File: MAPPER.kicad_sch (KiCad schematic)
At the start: 27 parts

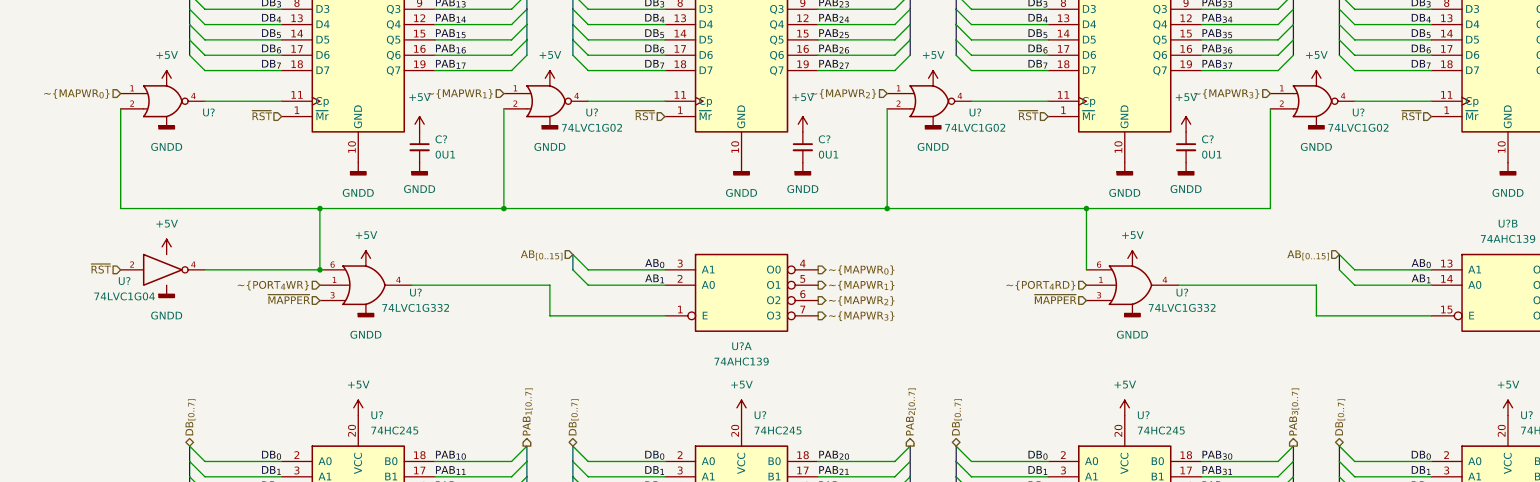
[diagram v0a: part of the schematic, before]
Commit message: distrustful of timing on reset of mapping registers
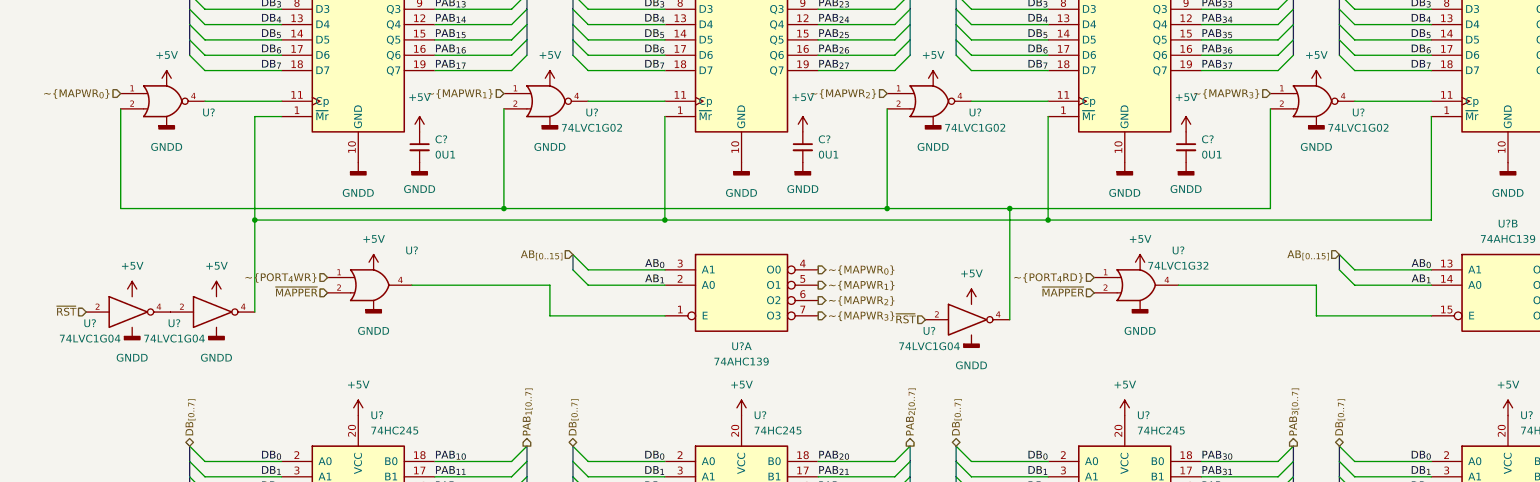
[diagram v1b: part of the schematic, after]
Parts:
- removed U? (x2): 74LVC1G332, symbol 74xGxx:74LVC1G332
- added U?: 74LVC1G32, symbol 74xGxx:74LVC1G32
- added U?: (no value), symbol 74xGxx:74LVC1G32
- added U? (x2): 74LVC1G04, symbol 74xGxx:74LVC1G04
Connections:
- net +5V: now also U?.5 (VCC), U?.5 (VCC), U?.5 (VCC), U?.5 (VCC)
- net GND: now also U?.3 (GND), U?.3 (GND), U?.3 (GND), U?.3 (GND)
- net ~{MAPPER}: now also U?.2, U?.2
- net ~{PORT_{4}RD}: now also U?.1
- net ~{PORT_{4}WR}: now also U?.1
- net ~{RST}: now also U?.2; no longer U?.1 (~{Mr}), U?.1 (~{Mr}), U?.1 (~{Mr}), U?.1 (~{Mr})
- net at U?.15 (E): now also U?.4
- net at U?.1 (E): now also U?.4
- new net: U?.1 (~{Mr}), U?.1 (~{Mr}), U?.1 (~{Mr}), U?.1 (~{Mr}), U?.4
- new net: U?.2, U?.4
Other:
- moved on the sheet: U?

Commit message: duh obvious optimization
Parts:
- removed U?: 74LVC1G04, symbol 74xGxx:74LVC1G04
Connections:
- net at U?.2, U?.2, U?.2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: now also U?.2, U?.4
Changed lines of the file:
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@@
   (junction (at 114.3 80.645) (diameter 0) (color 0 0 0 0)
   )
-  (junction (at 171.45 78.74) (diameter 0) (color 0 0 0 0)
-  )
   (junction (at 46.355 80.645) (diameter 0) (color 0 0 0 0)
   )
@@
   (junction (at 151.13 78.74) (diameter 0) (color 0 0 0 0)
   )
+  (junction (at 32.385 95.885) (diameter 0) (color 0 0 0 0)
+  )
+  (junction (at 32.385 78.74) (diameter 0) (color 0 0 0 0)
+  )
   (bus_entry (at 162.56 40.64) (size 2.54 2.54)
     (stroke (width 0) (type default) (color 0 0 0 0))
@@
     (stroke (width 0) (type default) (color 0 0 0 0))
   )
+  (wire (pts (xy 32.385 78.74) (xy 32.385 95.885))
+    (stroke (width 0) (type default) (color 0 0 0 0))
+  )
   (bus (pts (xy 35.56 118.11) (xy 35.56 120.65))
     (stroke (width 0) (type default) (color 0 0 0 0))
@@
     (stroke (width 0) (type default) (color 0 0 0 0))
   )
-  (wire (pts (xy 171.45 78.74) (xy 171.45 97.155))
-    (stroke (width 0) (type default) (color 0 0 0 0))
-  )
   (bus (pts (xy 218.44 133.35) (xy 218.44 135.89))
     (stroke (width 0) (type default) (color 0 0 0 0))
@@
     (stroke (width 0) (type default) (color 0 0 0 0))
   )
-  (wire (pts (xy 151.13 78.74) (xy 171.45 78.74))
-    (stroke (width 0) (type default) (color 0 0 0 0))
-  )
   (wire (pts (xy 241.3 123.19) (xy 228.6 123.19))
     (stroke (width 0) (type default) (color 0 0 0 0))
@@
     (stroke (width 0) (type default) (color 0 0 0 0))
   )
-  (wire (pts (xy 24.13 78.74) (xy 87.63 78.74))
+  (wire (pts (xy 24.13 78.74) (xy 32.385 78.74))
     (stroke (width 0) (type default) (color 0 0 0 0))
   )
@@
     (stroke (width 0) (type default) (color 0 0 0 0))
   )
+  (wire (pts (xy 32.385 78.74) (xy 87.63 78.74))
+    (stroke (width 0) (type default) (color 0 0 0 0))
+  )
   (wire (pts (xy 95.25 96.52) (xy 114.3 96.52))
     (stroke (width 0) (type default) (color 0 0 0 0))
@@
     (stroke (width 0) (type default) (color 0 0 0 0))
   )
-  (wire (pts (xy 171.45 78.74) (xy 214.63 78.74))
+  (wire (pts (xy 151.13 78.74) (xy 214.63 78.74))
     (stroke (width 0) (type default) (color 0 0 0 0))
   )
@@
   (hierarchical_label "DB_{[0..7]}" (shape bidirectional) (at 99.06 118.11 90)
     (effects (font (size 1.27 1.27)) (justify left))
-  )
-  (hierarchical_label "~{RST}" (shape input) (at 157.48 97.155 180)
-    (effects (font (size 1.27 1.27)) (justify right))
   )
   (symbol (lib_id "power:GNDD") (at 158.75 63.5 0) (unit 1)
@@
     )
     (property "Datasheet" "" (id 3) (at 200.66 148.59 0)
-      (effects (font (size 1.27 1.27)) hide)
-    )
-    (pin "1")
-  )
-  (symbol (lib_id "power:GNDD") (at 165.1 99.695 0) (unit 1)
-    (in_bom yes) (on_board yes) (fields_autoplaced)
-    (property "Reference" "#PWR?" (id 0) (at 165.1 106.045 0)
-      (effects (font (size 1.27 1.27)) hide)
-    )
-    (property "Value" "GNDD" (id 1) (at 165.1 104.775 0))
-    (property "Footprint" "" (id 2) (at 165.1 99.695 0)
-      (effects (font (size 1.27 1.27)) hide)
-    )
-    (property "Datasheet" "" (id 3) (at 165.1 99.695 0)
       (effects (font (size 1.27 1.27)) hide)
     )
@@
     (pin "1")
   )
-  (symbol (lib_id "74xGxx:74LVC1G04") (at 165.1 97.155 0) (unit 1)
-    (in_bom yes) (on_board yes)
-    (property "Reference" "U?" (id 0) (at 158.115 99.06 0))
-    (property "Value" "74LVC1G04" (id 1) (at 158.115 101.6 0))
-    (property "Footprint" "" (id 2) (at 165.1 97.155 0)
-      (effects (font (size 1.27 1.27)) hide)
-    )
-    (property "Datasheet" "http://www.ti.com/lit/sg/scyt129e/scyt129e.pdf" (id 3) (at 165.1 97.155 0)
-      (effects (font (size 1.27 1.27)) hide)
-    )
-    (pin "2")
-    (pin "3")
-    (pin "4")
-    (pin "5")
-  )
   (symbol (lib_id "power:+5V") (at 264.16 66.04 0) (unit 1)
     (in_bom yes) (on_board yes) (fields_autoplaced)
@@
       (effects (font (size 1.27 1.27)) hide)
     )
-    (pin "1")
-  )
-  (symbol (lib_id "power:+5V") (at 165.1 94.615 0) (unit 1)
-    (in_bom yes) (on_board yes) (fields_autoplaced)
-    (property "Reference" "#PWR?" (id 0) (at 165.1 98.425 0)
-      (effects (font (size 1.27 1.27)) hide)
-    )
-    (property "Value" "+5V" (id 1) (at 165.1 89.535 0))
-    (property "Footprint" "" (id 2) (at 165.1 94.615 0)
-      (effects (font (size 1.27 1.27)) hide)
-    )
-    (property "Datasheet" "" (id 3) (at 165.1 94.615 0)
-      (effects (font (size 1.27 1.27)) hide)
-    )

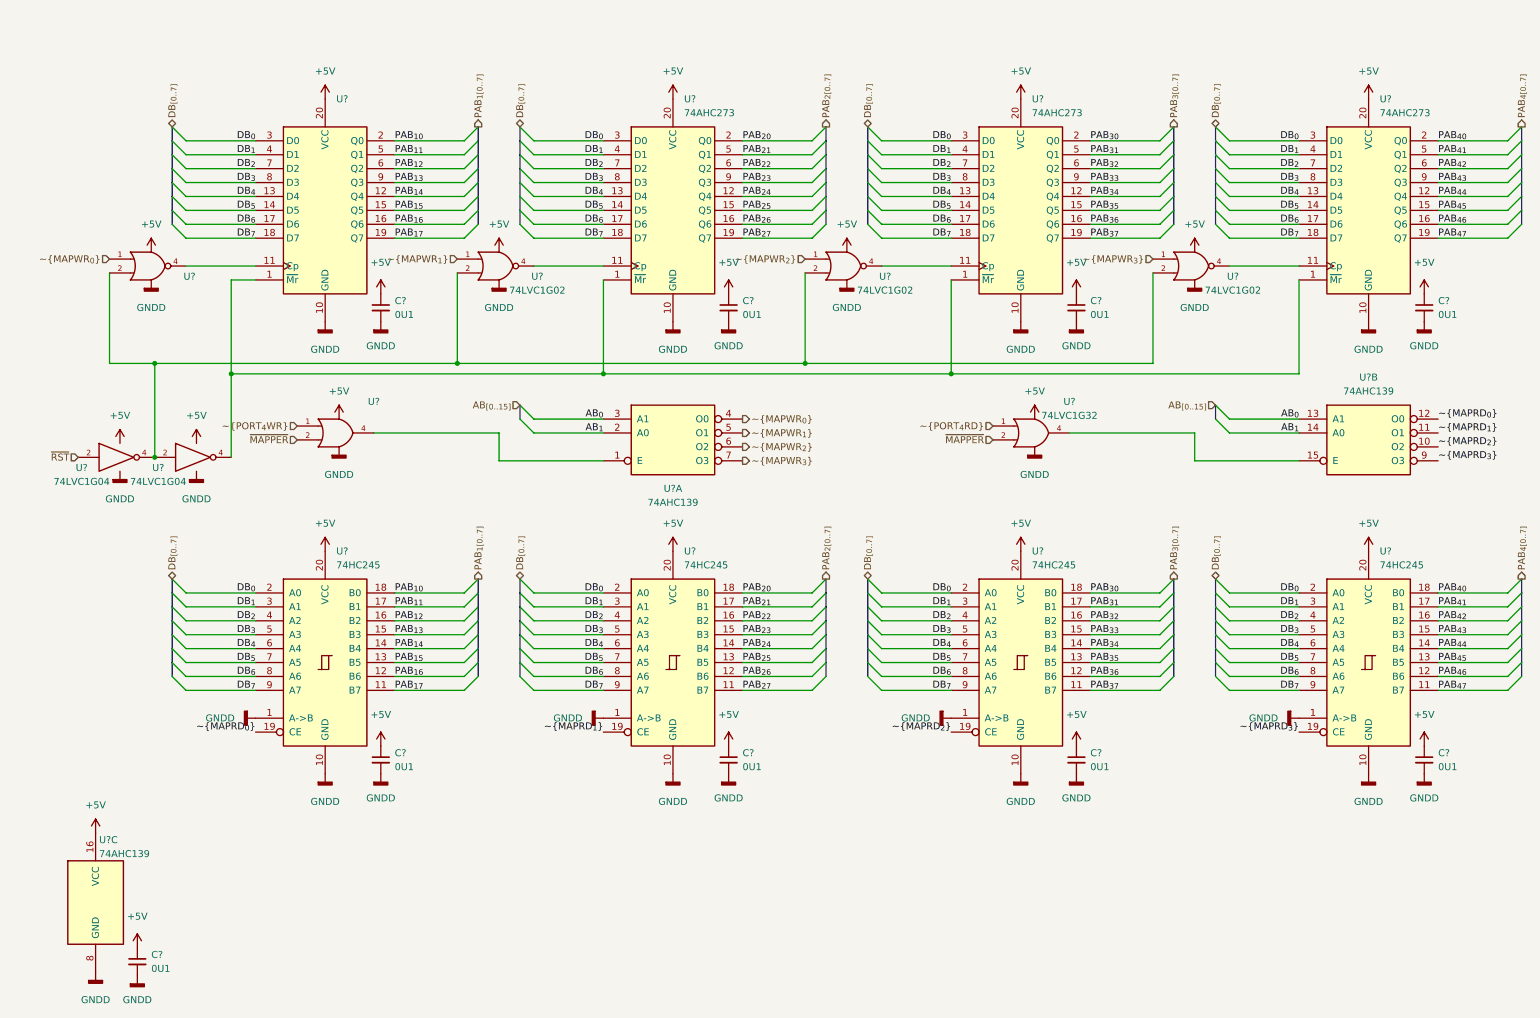
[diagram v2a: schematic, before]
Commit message: some clean up and simplification, as well as some renaming
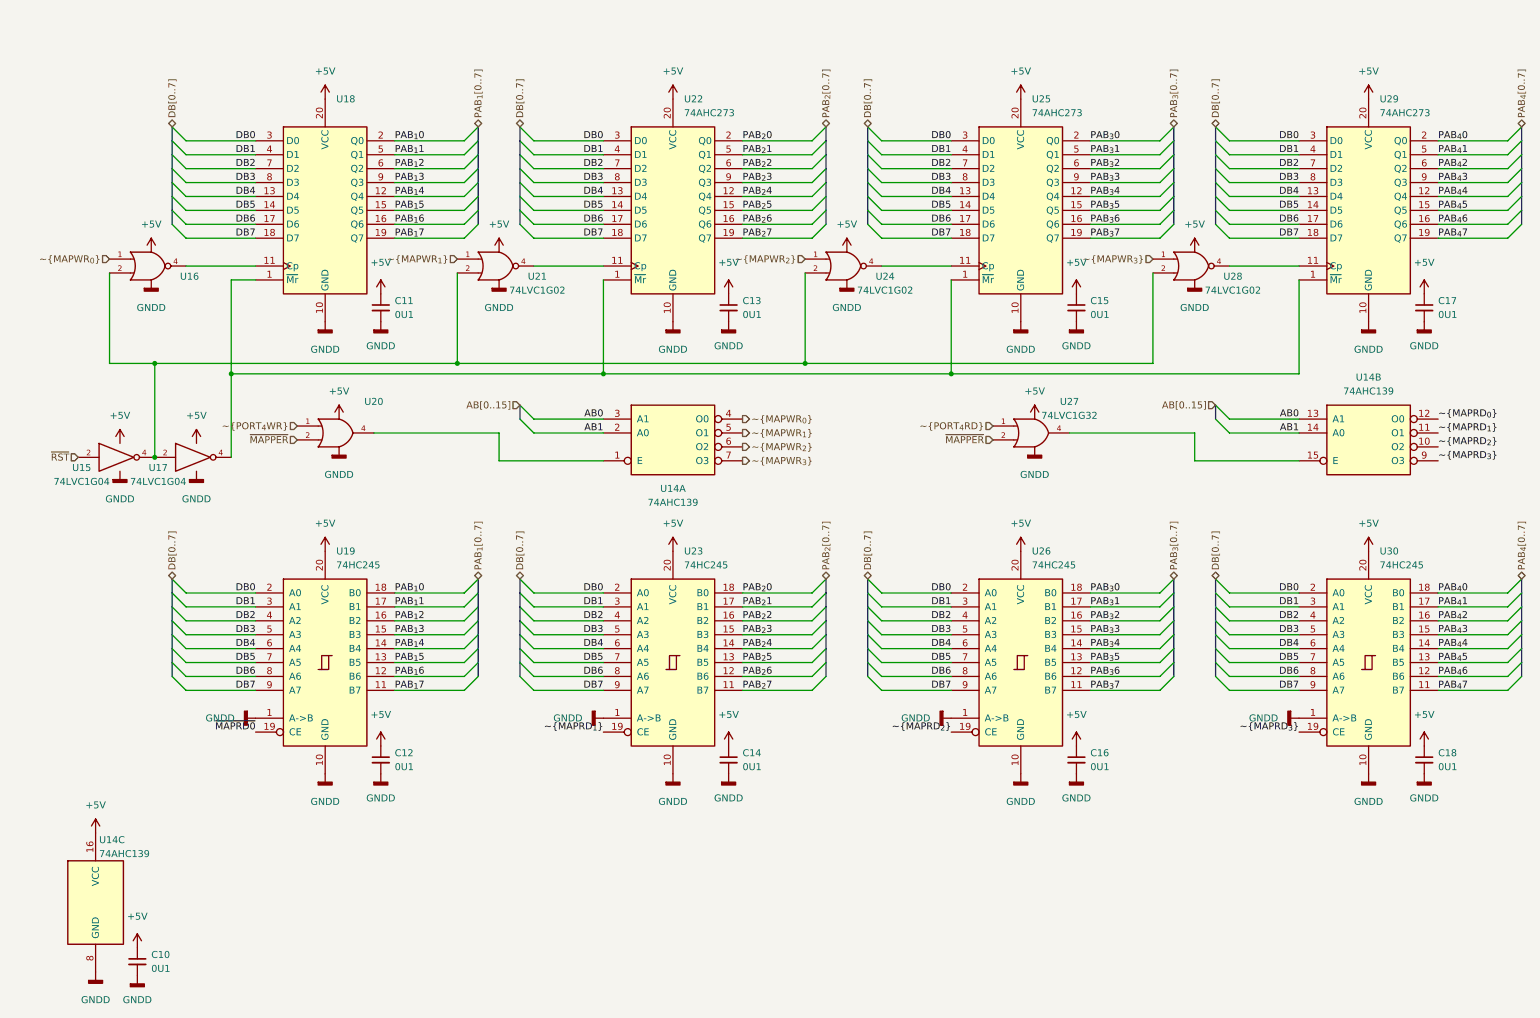
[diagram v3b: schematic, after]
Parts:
- gave numbers to parts that had none: 26
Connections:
- net ~{MAPRD_{0}}: no longer U19.19 (CE)
- net AB_{0} renamed AB0
- net AB_{1} renamed AB1
- net DB_{0} renamed DB0
- net DB_{1} renamed DB1
- net DB_{2} renamed DB2
- net DB_{3} renamed DB3
- net DB_{4} renamed DB4
- net DB_{5} renamed DB5
- net DB_{6} renamed DB6
- net DB_{7} renamed DB7
- net PAB_{1}_{0} renamed PAB_{1}0
- net PAB_{1}_{1} renamed PAB_{1}1
- net PAB_{1}_{2} renamed PAB_{1}2
- net PAB_{1}_{3} renamed PAB_{1}3
- net PAB_{1}_{4} renamed PAB_{1}4
- net PAB_{1}_{5} renamed PAB_{1}5
- net PAB_{1}_{6} renamed PAB_{1}6
- net PAB_{1}_{7} renamed PAB_{1}7
- net PAB_{2}_{0} renamed PAB_{2}0
- net PAB_{2}_{1} renamed PAB_{2}1
- net PAB_{2}_{2} renamed PAB_{2}2
- net PAB_{2}_{3} renamed PAB_{2}3
- net PAB_{2}_{4} renamed PAB_{2}4
- net PAB_{2}_{5} renamed PAB_{2}5
- net PAB_{2}_{6} renamed PAB_{2}6
- net PAB_{2}_{7} renamed PAB_{2}7
- net PAB_{3}_{0} renamed PAB_{3}0
- net PAB_{3}_{1} renamed PAB_{3}1
- net PAB_{3}_{2} renamed PAB_{3}2
- net PAB_{3}_{3} renamed PAB_{3}3
- net PAB_{3}_{4} renamed PAB_{3}4
- net PAB_{3}_{5} renamed PAB_{3}5
- net PAB_{3}_{6} renamed PAB_{3}6
- net PAB_{3}_{7} renamed PAB_{3}7
- net PAB_{4}_{0} renamed PAB_{4}0
- net PAB_{4}_{1} renamed PAB_{4}1
- net PAB_{4}_{2} renamed PAB_{4}2
- net PAB_{4}_{3} renamed PAB_{4}3
- net PAB_{4}_{4} renamed PAB_{4}4
- net PAB_{4}_{5} renamed PAB_{4}5
- net PAB_{4}_{6} renamed PAB_{4}6
- net PAB_{4}_{7} renamed PAB_{4}7
- new net ~{MAPRD0}: U19.19 (CE)
